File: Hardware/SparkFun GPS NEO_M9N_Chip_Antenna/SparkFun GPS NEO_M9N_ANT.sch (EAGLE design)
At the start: 51 parts, among them J13 U.FL, J2 Qwiic Right Angle, J4 Qwiic Right Angle, U1 U-BLOX_NEO-M9N, U2 3.3V

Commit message: Beings work on version with antenna
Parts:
- removed J13: U.FL, SparkFun-Connectors:U.FL2PIN
- added Y1: GPS_CHIP_ANTENNAW3011, SparkFun-GPS:GPS_CHIP_ANTENNAW3011
- LED1: value Yellow -> BLUE; device SparkFun-LED:LED-YELLOW0603 -> SparkFun-LED:LED-BLUE0603
- renumbered JP1 to PPS, JP2 to PWR\, JP4 to SPI
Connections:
- net GND: now also Y1.GND; no longer J13.GND
- net GPS_ANT1: now also Y1.SIGNAL; no longer J13.SIGNAL
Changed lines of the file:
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@@
 <part name="SUPPLY9" library="SparkFun-PowerSymbols" deviceset="3.3V" device=""/>
 <part name="GND4" library="SparkFun-PowerSymbols" deviceset="GND" device=""/>
-<part name="LED1" library="SparkFun-LED" deviceset="LED-YELLOW" device="0603" value="Yellow"/>
-<part name="JP1" library="SparkFun-Jumpers" deviceset="JUMPER-SMT_2_NC_TRACE" device="_SILK" value="JUMPER-SMT_2_NC_TRACE_SILK"/>
+<part name="LED1" library="SparkFun-LED" deviceset="LED-BLUE" device="0603" value="BLUE"/>
+<part name="PPS" library="SparkFun-Jumpers" deviceset="JUMPER-SMT_2_NC_TRACE" device="_SILK" value="JUMPER-SMT_2_NC_TRACE_SILK"/>
 <part name="D2" library="SparkFun-DiscreteSemi" deviceset="DIODE-SCHOTTKY" device="-PMEG4005EJ" value="0.5A/40V/420mV"/>
 <part name="SUPPLY5" library="SparkFun-PowerSymbols" deviceset="3.3V" device=""/>
@@
 <part name="GND15" library="SparkFun-PowerSymbols" deviceset="GND" device=""/>
 <part name="GND27" library="SparkFun-PowerSymbols" deviceset="GND" device=""/>
-<part name="J13" library="SparkFun-Connectors" deviceset="U.FL2PIN" device="" value="U.FL"/>
 <part name="C4" library="SparkFun-Capacitors" deviceset="1.0UF" device="-0603-16V-10%" value="1.0uF"/>
 <part name="GND11" library="SparkFun-PowerSymbols" deviceset="GND" device=""/>
@@
 <part name="R9" library="SparkFun-Resistors" deviceset="27OHM" device="-0603-1/10W-1%" value="27"/>
 <part name="R10" library="SparkFun-Resistors" deviceset="27OHM" device="-0603-1/10W-1%" value="27"/>
-<part name="JP4" library="SparkFun-Jumpers" deviceset="JUMPER-SMT_2_NO" device="_SILK" value="JUMPER-SMT_2_NO_SILK"/>
+<part name="SPI" library="SparkFun-Jumpers" deviceset="JUMPER-SMT_2_NO" device="_SILK" value="JUMPER-SMT_2_NO_SILK"/>
 <part name="GND2" library="SparkFun-PowerSymbols" deviceset="GND" device=""/>
 <part name="C1" library="SparkFun-Capacitors" deviceset="47PF" device="-0603-50V-5%" value="47pF"/>
@@
 <part name="LOGO2" library="SparkFun-Aesthetics" deviceset="SFE_LOGO_NAME_FLAME" device=".1_INCH"/>
 <part name="U1" library="gps" deviceset="U-BLOX_NEO-M9N" device=""/>
-<part name="JP2" library="SparkFun-Jumpers" deviceset="JUMPER-SMT_2_NC_TRACE" device="_SILK" value="JUMPER-SMT_2_NC_TRACE_SILK"/>
+<part name="PWR\" library="SparkFun-Jumpers" deviceset="JUMPER-SMT_2_NC_TRACE" device="_SILK" value="JUMPER-SMT_2_NC_TRACE_SILK"/>
 <part name="D3" library="SparkFun-IC-Power" deviceset="PRTR5V0U2" device="F"/>
 <part name="J5" library="SparkFun-Connectors" deviceset="CONN_04" device="1X04_NO_SILK"/>
@@
 <part name="R16" library="SparkFun-Resistors" deviceset="10KOHM" device="-0402-1/16W-1%" value="10k"/>
 <part name="SUPPLY12" library="SparkFun-PowerSymbols" deviceset="3.3V" device=""/>
+<part name="Y1" library="SparkFun-GPS" deviceset="GPS_CHIP_ANTENNA" device="W3011"/>
 </parts>
 <sheets>
@@
 <text x="43.18" y="12.7" size="1.778" layer="97" font="vector">Close jumper to
 enable SPI</text>
-<text x="215.392" y="104.14" size="1.778" layer="97" font="vector">CI160808-33NJ</text>
+<text x="215.392" y="111.76" size="1.778" layer="97" font="vector">CI160808-33NJ</text>
 <text x="166.624" y="11.176" size="2.54" layer="94" font="vector">Elias Santistevan</text>
 <text x="78.74" y="99.06" size="2.54" layer="94" font="vector">Headers</text>
@@
 <attribute name="VALUE" x="20.955" y="8.382" size="1.778" layer="96" font="vector" rot="R90" align="top-left"/>
 </instance>
-<instance part="JP1" gate="G$1" x="20.32" y="40.64" smashed="yes" rot="R90">
+<instance part="PPS" gate="G$1" x="20.32" y="40.64" smashed="yes" rot="R90">
 <attribute name="NAME" x="19.558" y="45.339" size="1.778" layer="95" font="vector" rot="R180"/>
 </instance>
@@
 <attribute name="VALUE" x="129.54" y="127" size="1.778" layer="96" font="vector"/>
 </instance>
-<instance part="GND27" gate="1" x="210.82" y="71.12" smashed="yes">
-<attribute name="VALUE" x="210.82" y="70.866" size="1.778" layer="96" font="vector" align="top-center"/>
-</instance>
-<instance part="J13" gate="G$1" x="210.82" y="101.6" smashed="yes">
-<attribute name="NAME" x="202.565" y="101.473" size="1.778" layer="95" font="vector"/>
-<attribute name="VALUE" x="202.438" y="98.806" size="1.778" layer="96" font="vector"/>
+<instance part="GND27" gate="1" x="213.36" y="71.12" smashed="yes">
+<attribute name="VALUE" x="213.36" y="70.866" size="1.778" layer="96" font="vector" align="top-center"/>
 </instance>
 <instance part="C4" gate="G$1" x="228.6" y="154.94" smashed="yes">
@@
 <attribute name="VALUE" x="19.812" y="134.874" size="1.778" layer="96" font="vector" rot="R180" align="top-center"/>
 </instance>
-<instance part="JP4" gate="G$1" x="40.64" y="17.78" smashed="yes" rot="R90">
+<instance part="SPI" gate="G$1" x="40.64" y="17.78" smashed="yes" rot="R90">
 <attribute name="NAME" x="48.26" y="20.32" size="1.778" layer="95" font="vector" rot="R180"/>
 </instance>
@@
 <attribute name="VALUE" x="35.56" y="124.46" size="1.778" layer="96" font="vector"/>
 </instance>
-<instance part="JP2" gate="G$1" x="12.7" y="40.64" smashed="yes" rot="R90">
+<instance part="PWR\" gate="G$1" x="12.7" y="40.64" smashed="yes" rot="R90">
 <attribute name="NAME" x="11.938" y="45.339" size="1.778" layer="95" font="vector" rot="R180"/>
 </instance>
@@
 <instance part="SUPPLY12" gate="G$1" x="40.64" y="40.64" smashed="yes">
 <attribute name="VALUE" x="40.64" y="43.434" size="1.778" layer="96" font="vector" align="bottom-center"/>
+</instance>
+<instance part="Y1" gate="G$1" x="210.82" y="114.3" smashed="yes">
+<attribute name="NAME" x="213.868" y="109.22" size="1.778" layer="95" font="vector"/>
+<attribute name="VALUE" x="213.868" y="106.934" size="1.778" layer="96" font="vector"/>
 </instance>
 </instances>
@@
 </segment>
 <segment>
-<pinref part="JP2" gate="G$1" pin="2"/>
+<pinref part="PWR\" gate="G$1" pin="2"/>
 <pinref part="P+1" gate="G$1" pin="3.3V"/>
 <wire x1="12.7" y1="45.72" x2="12.7" y2="48.26" width="0.1524" layer="91"/>
@@
 </segment>
 <segment>
-<pinref part="J13" gate="G$1" pin="GND"/>
-<pinref part="GND27" gate="1" pin="GND"/>
-<wire x1="210.82" y1="73.66" x2="210.82" y2="96.52" width="0.1524" layer="91"/>
-</segment>
-<segment>
 <wire x1="228.6" y1="132.08" x2="228.6" y2="152.4" width="0.1524" layer="91"/>
 <pinref part="C4" gate="G$1" pin="2"/>
@@
 </segment>
 <segment>
-<pinref part="JP4" gate="G$1" pin="1"/>
+<pinref part="SPI" gate="G$1" pin="1"/>
 <wire x1="40.64" y1="12.7" x2="40.64" y2="10.16" width="0.1524" layer="91"/>
 <pinref part="GND2" gate="1" pin="GND"/>
@@
 <wire x1="139.7" y1="134.62" x2="139.7" y2="132.08" width="0.1524" layer="91"/>
 </segment>
+<segment>
+<pinref part="Y1" gate="G$1" pin="GND"/>
+<wire x1="213.36" y1="104.14" x2="213.36" y2="73.66" width="0.1524" layer="91"/>
+<pinref part="GND27" gate="1" pin="GND"/>
+</segment>
 </net>
 <net name="SCL/SCK" class="0">
@@
 <wire x1="20.32" y1="45.72" x2="20.32" y2="48.26" width="0.1524" layer="91"/>
 <label x="20.32" y="48.26" size="1.27" layer="95" font="vector" rot="R90" xref="yes"/>
-<pinref part="JP1" gate="G$1" pin="2"/>
+<pinref part="PPS" gate="G$1" pin="2"/>
 </segment>
 </net>
@@
 <net name="N$4" class="0">
 <segment>
-<pinref part="JP1" gate="G$1" pin="1"/>
+<pinref part="PPS" gate="G$1" pin="1"/>
 <pinref part="R11" gate="G$1" pin="2"/>
 <wire x1="20.32" y1="35.56" x2="20.32" y2="33.02" width="0.1524" layer="91"/>
@@
 <net name="GPS_ANT1" class="0">
 <segment>
-<wire x1="218.44" y1="101.6" x2="215.9" y2="101.6" width="0.1524" layer="91"/>
-<pinref part="J13" gate="G$1" pin="SIGNAL"/>
 <wire x1="218.44" y1="101.6" x2="218.44" y2="99.06" width="0.1524" layer="91"/>
 <pinref part="FB1" gate="G$1" pin="1"/>
@@
 <junction x="218.44" y="101.6"/>
 <label x="223.52" y="101.6" size="1.27" layer="95" xref="yes"/>
+<wire x1="210.82" y1="101.6" x2="218.44" y2="101.6" width="0.1524" layer="91"/>
+<wire x1="210.82" y1="101.6" x2="210.82" y2="104.14" width="0.1524" layer="91"/>
+<pinref part="Y1" gate="G$1" pin="SIGNAL"/>
 </segment>
 <segment>
@@
 <segment>
 <pinref part="R16" gate="G$1" pin="1"/>
-<pinref part="JP4" gate="G$1" pin="2"/>
+<pinref part="SPI" gate="G$1" pin="2"/>
 <wire x1="40.64" y1="27.94" x2="40.64" y2="25.4" width="0.1524" layer="91"/>
 <wire x1="40.64" y1="25.4" x2="40.64" y2="22.86" width="0.1524" layer="91"/>
@@
 <net name="N$1" class="0">
 <segment>
-<pinref part="JP2" gate="G$1" pin="1"/>
+<pinref part="PWR\" gate="G$1" pin="1"/>
 <pinref part="R1" gate="G$1" pin="2"/>
 <wire x1="12.7" y1="35.56" x2="12.7" y2="33.02" width="0.1524" layer="91"/>

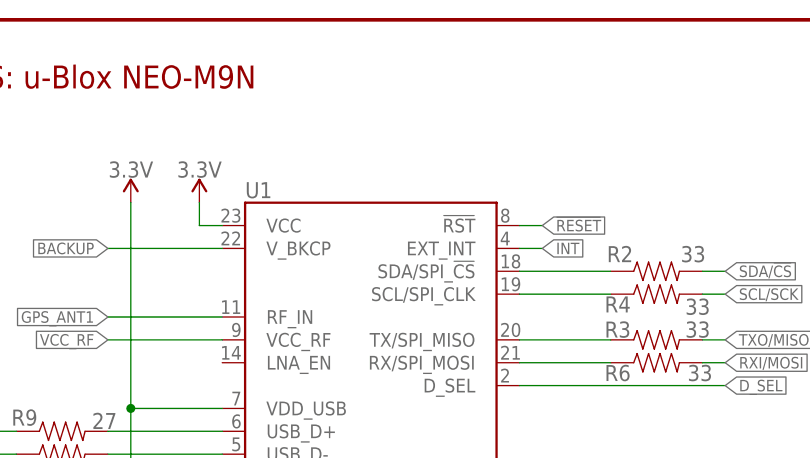
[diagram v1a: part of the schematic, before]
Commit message: Changes trace for antenna to s-bend, adds silk to battery, adds vcc range to schematic, adjusts jumper
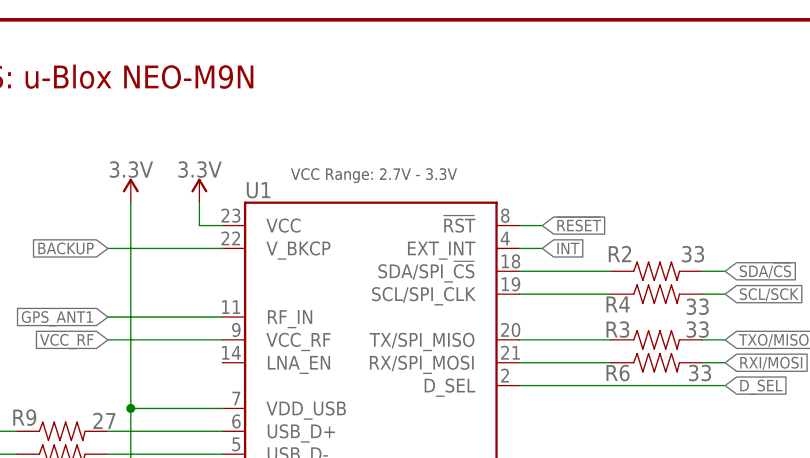
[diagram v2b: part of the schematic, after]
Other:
- note added: "VCC Range: 2.7V - 3.3V"
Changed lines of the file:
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@@
 <class number="2" name="3.3V" width="0.508" drill="0">
+</class>
+<class number="3" name="Antenna" width="1" drill="0">
+<clearance class="3" value="0.3"/>
 </class>
 </classes>
@@
 <text x="104.14" y="177.8" size="2.54" layer="94" font="vector">USB Connector - Power</text>
 <text x="148.844" y="6.604" size="2.54" layer="94" font="vector">Based on design by: Nathan Seidle</text>
+<text x="40.64" y="167.64" size="1.27" layer="97" font="vector">VCC Range: 2.7V - 3.3V</text>
 </plain>
 <instances>
@@
 </segment>
 </net>
-<net name="GPS_ANT1" class="0">
+<net name="GPS_ANT1" class="3">
 <segment>
 <wire x1="218.44" y1="101.6" x2="218.44" y2="99.06" width="0.1524" layer="91"/>
